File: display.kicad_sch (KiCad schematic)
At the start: 3 parts, among them J2 Display_shield

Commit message: -add some changes to power section and display
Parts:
- removed C4: 100n, Capacitor_SMD:C_0603_1608Metric_Pad1.08x0.95mm_HandSolder, symbol Device:C_Small
- removed J2: Display_shield, Connector_PinHeader_2.54mm:PinHeader_2x13_P2.54mm_Vertical_SMD, symbol Connector_Generic:Conn_02x13_Odd_Even
- added C21, C22, C23: 100n, Capacitor_SMD:C_0603_1608Metric_Pad1.08x0.95mm_HandSolder, symbol Device:C_Small
- added J1: Touch, Connector_FFC-FPC:TE_0-1734839-6_1x06-1MP_P0.5mm_Horizontal, symbol Connector:Conn_01x06_Pin
- added J11: FPC_40P_LCD_ILI9488, Connector_FFC-FPC:TE_4-1734839-0_1x40-1MP_P0.5mm_Horizontal, symbol Connector:Conn_01x40_Male
- added J12: Display, Connector_PinHeader_2.54mm:PinHeader_2x05_P2.54mm_Vertical_SMD, symbol Connector_Generic:Conn_02x05_Odd_Even
- added J9: Conn_02x02_Odd_Even, Connector_PinHeader_2.54mm:PinHeader_2x02_P2.54mm_Vertical_SMD, symbol Connector_Generic:Conn_02x02_Odd_Even
- added R28, R33: dnp, Resistor_SMD:R_0603_1608Metric_Pad0.98x0.95mm_HandSolder, symbol Device:R
- added R39, R40, R41: 220, Resistor_SMD:R_0603_1608Metric_Pad0.98x0.95mm_HandSolder, symbol Device:R
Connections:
- net +3.3V: now also C3.2, C21.1, C23.2, J1.1 (Pin_1), J11.33 (Pin_33), J11.6 (Pin_6), J11.7 (Pin_7), J12.7 (Pin_7), R33.2; no longer C3.1
- net +5V: now also C22.1, J12.9 (Pin_9)
- net Display_CS: now also J11.9 (Pin_9), J12.4 (Pin_4)
- net Display_DC: now also J11.11 (Pin_11), J12.5 (Pin_5)
- net Display_RST: now also J11.15 (Pin_15), J12.6 (Pin_6)
- net Display_TP_IRQ: now also J1.4 (Pin_4), J9.3 (Pin_3)
- net GND: now also C3.1, C21.2, C22.2, C23.1, J1.6 (Pin_6), J11.12 (Pin_12), J11.16 (Pin_16), J11.17 (Pin_17), J11.18 (Pin_18), J11.19 (Pin_19), J11.20 (Pin_20), J11.21 (Pin_21), J11.22 (Pin_22), J11.23 (Pin_23), J11.24 (Pin_24), J11.25 (Pin_25), J11.26 (Pin_26), J11.27 (Pin_27), J11.28 (Pin_28), J11.29 (Pin_29), J11.30 (Pin_30), J11.31 (Pin_31), J11.32 (Pin_32), J11.37 (Pin_37), J11.38 (Pin_38), J11.39 (Pin_39), J11.40 (Pin_40), J11.5 (Pin_5), J12.10 (Pin_10), R28.1, R39.2, R40.2, R41.2; no longer C3.2
- net SPI_CLK: now also J11.10 (Pin_10), J12.2 (Pin_2)
- net SPI_MISO: now also J12.1 (Pin_1)
- net SPI_MOSI: now also J11.13 (Pin_13), J12.3 (Pin_3)
- new net: J11.34 (Pin_34), R39.1
- new net: J11.35 (Pin_35), R40.1
- new net: J11.36 (Pin_36), R41.1
- new net: J12.8 (Pin_8), R28.2, R33.1
- new net Display_TP_RST: J1.5 (Pin_5), J9.1 (Pin_1)
- new net TP_SCL: J1.3 (Pin_3), J9.4 (Pin_4)
- new net TP_SDA: J1.2 (Pin_2), J9.2 (Pin_2)
- no-connect marks 9 -> 6

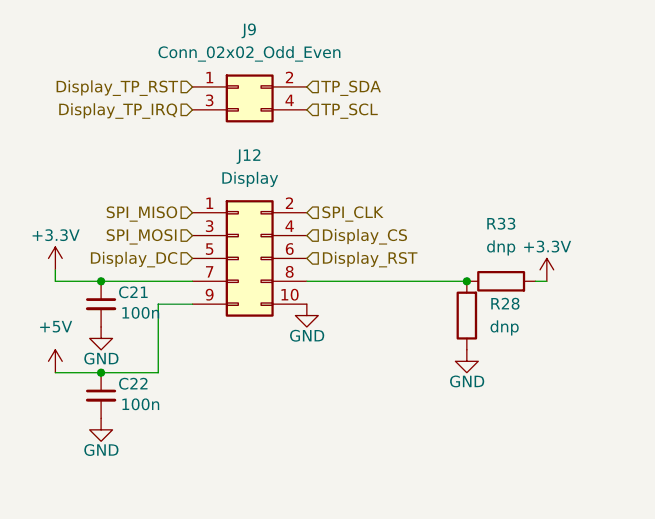
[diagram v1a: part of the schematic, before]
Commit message: -enh repin mcu in schematic
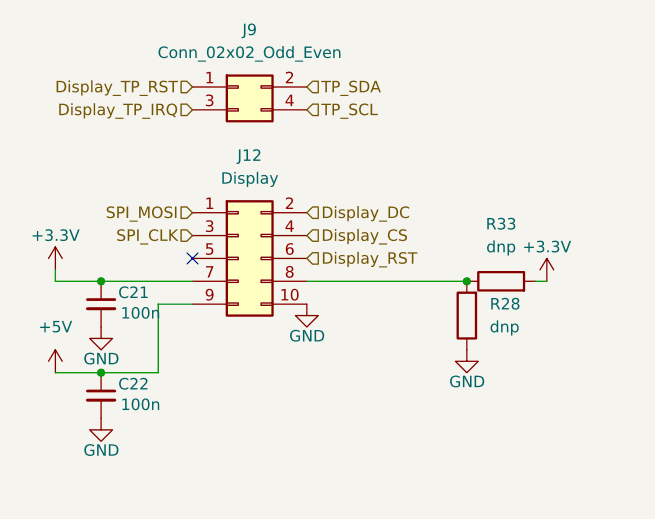
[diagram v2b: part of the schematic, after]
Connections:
- net SPI_MISO is gone; now on net SPI_MOSI: J12.1 (Pin_1)
- net Display_DC: now also J12.2 (Pin_2); no longer J12.5 (Pin_5)
- net SPI_CLK: now also J12.3 (Pin_3); no longer J12.2 (Pin_2)
- net SPI_MOSI: no longer J12.3 (Pin_3)
- no-connect marks 6 -> 7
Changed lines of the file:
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@@
+	)
+	(no_connect
+		(at 100.33 49.53)
 	)
 	(no_connect
@@
 	(hierarchical_label "SPI_CLK"
 		(shape input)
+		(at 100.33 46.99 180)
+		(fields_autoplaced yes)
+		(effects
+			(font
+				(size 1.27 1.27)
+			)
+			(justify right)
+		)
+	)
+	(hierarchical_label "SPI_MOSI"
+		(shape input)
+		(at 215.9 62.23 0)
+		(fields_autoplaced yes)
+		(effects
+			(font
+				(size 1.27 1.27)
+			)
+			(justify left)
+		)
+	)
+	(hierarchical_label "SPI_CLK"
+		(shape input)
+		(at 215.9 54.61 0)
+		(fields_autoplaced yes)
+		(effects
+			(font
+				(size 1.27 1.27)
+			)
+			(justify left)
+		)
+	)
+	(hierarchical_label "TP_SDA"
+		(shape input)
+		(at 113.03 30.48 0)
+		(fields_autoplaced yes)
+		(effects
+			(font
+				(size 1.27 1.27)
+			)
+			(justify left)
+		)
+	)
+	(hierarchical_label "SPI_MOSI"
+		(shape input)
+		(at 100.33 44.45 180)
+		(fields_autoplaced yes)
+		(effects
+			(font
+				(size 1.27 1.27)
+			)
+			(justify right)
+		)
+	)
+	(hierarchical_label "TP_SCL"
+		(shape input)
+		(at 173.99 78.74 0)
+		(fields_autoplaced yes)
+		(effects
+			(font
+				(size 1.27 1.27)
+			)
+			(justify left)
+		)
+	)
+	(hierarchical_label "TP_SCL"
+		(shape input)
+		(at 113.03 33.02 0)
+		(fields_autoplaced yes)
+		(effects
+			(font
+				(size 1.27 1.27)
+			)
+			(justify left)
+		)
+	)
+	(hierarchical_label "TP_SDA"
+		(shape input)
+		(at 173.99 76.2 0)
+		(fields_autoplaced yes)
+		(effects
+			(font
+				(size 1.27 1.27)
+			)
+			(justify left)
+		)
+	)
+	(hierarchical_label "Display_RST"
+		(shape input)
+		(at 113.03 49.53 0)
+		(fields_autoplaced yes)
+		(effects
+			(font
+				(size 1.27 1.27)
+			)
+			(justify left)
+		)
+	)
+	(hierarchical_label "Display_TP_RST"
+		(shape input)
+		(at 173.99 83.82 0)
+		(fields_autoplaced yes)
+		(effects
+			(font
+				(size 1.27 1.27)
+			)
+			(justify left)
+		)
+	)
+	(hierarchical_label "Display_TP_IRQ"
+		(shape input)
+		(at 100.33 33.02 180)
+		(fields_autoplaced yes)
+		(effects
+			(font
+				(size 1.27 1.27)
+			)
+			(justify right)
+		)
+	)
+	(hierarchical_label "Display_TP_IRQ"
+		(shape input)
+		(at 173.99 81.28 0)
+		(fields_autoplaced yes)
+		(effects
+			(font
+				(size 1.27 1.27)
+			)
+			(justify left)
+		)
+	)
+	(hierarchical_label "Display_DC"
+		(shape input)
 		(at 113.03 44.45 0)
 		(fields_autoplaced yes)
@@
 		)
 	)
-	(hierarchical_label "SPI_MOSI"
-		(shape input)
-		(at 215.9 62.23 0)
-		(fields_autoplaced yes)
-		(effects
-			(font
-				(size 1.27 1.27)
-			)
-			(justify left)
-		)
-	)
-	(hierarchical_label "SPI_CLK"
-		(shape input)
-		(at 215.9 54.61 0)
-		(fields_autoplaced yes)
-		(effects
-			(font
-				(size 1.27 1.27)
-			)
-			(justify left)
-		)
-	)
-	(hierarchical_label "TP_SDA"
-		(shape input)
-		(at 113.03 30.48 0)
-		(fields_autoplaced yes)
-		(effects
-			(font
-				(size 1.27 1.27)
-			)
-			(justify left)
-		)
-	)
-	(hierarchical_label "SPI_MOSI"
-		(shape input)
-		(at 100.33 46.99 180)
-		(fields_autoplaced yes)
-		(effects
-			(font
-				(size 1.27 1.27)
-			)
-			(justify right)
-		)
-	)
-	(hierarchical_label "TP_SCL"
-		(shape input)
-		(at 173.99 78.74 0)
-		(fields_autoplaced yes)
-		(effects
-			(font
-				(size 1.27 1.27)
-			)
-			(justify left)
-		)
-	)
-	(hierarchical_label "TP_SCL"
-		(shape input)
-		(at 113.03 33.02 0)
-		(fields_autoplaced yes)
-		(effects
-			(font
-				(size 1.27 1.27)
-			)
-			(justify left)
-		)
-	)
-	(hierarchical_label "TP_SDA"
-		(shape input)
-		(at 173.99 76.2 0)
-		(fields_autoplaced yes)
-		(effects
-			(font
-				(size 1.27 1.27)
-			)
-			(justify left)
-		)
-	)
-	(hierarchical_label "Display_RST"
-		(shape input)
-		(at 113.03 49.53 0)
-		(fields_autoplaced yes)
-		(effects
-			(font
-				(size 1.27 1.27)
-			)
-			(justify left)
-		)
-	)
-	(hierarchical_label "Display_TP_RST"
-		(shape input)
-		(at 173.99 83.82 0)
-		(fields_autoplaced yes)
-		(effects
-			(font
-				(size 1.27 1.27)
-			)
-			(justify left)
-		)
-	)
-	(hierarchical_label "Display_TP_IRQ"
-		(shape input)
-		(at 100.33 33.02 180)
-		(fields_autoplaced yes)
-		(effects
-			(font
-				(size 1.27 1.27)
-			)
-			(justify right)
-		)
-	)
-	(hierarchical_label "SPI_MISO"
-		(shape input)
-		(at 100.33 44.45 180)
-		(fields_autoplaced yes)
-		(effects
-			(font
-				(size 1.27 1.27)
-			)
-			(justify right)
-		)
-	)
-	(hierarchical_label "Display_TP_IRQ"
-		(shape input)
-		(at 173.99 81.28 0)
-		(fields_autoplaced yes)
-		(effects
-			(font
-				(size 1.27 1.27)
-			)
-			(justify left)
-		)
-	)
-	(hierarchical_label "Display_DC"
-		(shape input)
-		(at 100.33 49.53 180)
-		(fields_autoplaced yes)
-		(effects
-			(font
-				(size 1.27 1.27)
-			)
-			(justify right)
-		)
-	)

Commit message: -add end revision
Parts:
- removed C23, C3: 100n, Capacitor_SMD:C_0603_1608Metric_Pad1.08x0.95mm_HandSolder, symbol Device:C_Small
- removed J11: FPC_40P_LCD_ILI9488, Connector_FFC-FPC:TE_4-1734839-0_1x40-1MP_P0.5mm_Horizontal, symbol Connector:Conn_01x40_Male
- removed R39, R40, R41: 220, Resistor_SMD:R_0603_1608Metric_Pad0.98x0.95mm_HandSolder, symbol Device:R
- added C25, C26: 100n, Capacitor_SMD:C_0603_1608Metric_Pad1.08x0.95mm_HandSolder, symbol Device:C_Small
- added J14: 62684-402100AHLF, lib:62684402100AHLF, symbol 62684-402100AHLF:62684-402100AHLF
- added R45, R46, R47: 10k, Resistor_SMD:R_0603_1608Metric_Pad0.98x0.95mm_HandSolder, symbol Device:R
- added R48, R49, R50: 220, Resistor_SMD:R_0603_1608Metric_Pad0.98x0.95mm_HandSolder, symbol Device:R
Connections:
- net +3.3V: now also C25.2, C26.2, J14.34, J14.35, J14.8, R45.2, R46.2, R47.2
- net Display_CS: now also J14.32
- net Display_DC: now also J14.31
- net Display_RST: now also J14.26
- net GND: now also C25.1, C26.1, J14.10, J14.11, J14.12, J14.13, J14.14, J14.15, J14.16, J14.17, J14.18, J14.19, J14.20, J14.21, J14.22, J14.23, J14.24, J14.25, J14.36, J14.4, J14.9, J14.MP1, J14.MP2, R48.2, R49.2, R50.2
- net SPI_CLK: now also J14.30
- net SPI_MOSI: now also J14.28
- net SPI_MISO: now reaches J12.5 (Pin_5)
- net SPI_MISO: now also J14.27
- new net: J14.5, R48.1
- new net: J14.3, R47.1
- new net: J14.2, R46.1
- new net: J14.7, R50.1
- new net: J14.1, R45.1
- new net: J14.6, R49.1
- no-connect marks 7 -> 6
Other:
- moved on the sheet: J1
